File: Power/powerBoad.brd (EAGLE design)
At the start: 160 x 100 mm, 26 parts, among them CON1 MR30PW-M, CON2 XT30PW-M, CON3 XT30PW-M, U1 V7805-1000, U2 LD1117S33CTR, X1 JST-XH-06-PIN-LONG-PAD, X2 JST-XH-06-PIN-LONG-PAD, X3 JST-XH-06-PIN-LONG-PAD, X4 JST-XH-06-PIN-LONG-PAD

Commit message: some update 部品配置
# ==== Emojis ====
# ✨ :sparkles: Add new feature
# ✅  :white_check_mark: Update existing feature (not bug)
# ⚠️  :warning: Fix bug/error
# 🔥  :fire: Remove files or features
# ✏️ :pencil2: Fix typos
# 📝  :memo: Update documentation
# ♻️  :recycle: Dependencies update
# 🐧  :penguin: Improved the Linux
# 🍎  :apple: Improved the macOS
# 🔖 :bookmark: Add new library
# 🎉  :tada: Initial commit

# ==== Format ====
# :emoji: Subject
#
# Commit body...

# ==== Messages ====
# 新規(ファイル)機能追加: Add
# 機能修正、既存機能追加（バグではない): Update
# リファクタリング: Clean
# ファイル名変更:
# 削除など: Remove
# バグ修正: Fix
# バージョンアップ: Upgrade
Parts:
- removed J1: (no value), SparkFun-Connectors:JST-5-PTH
- removed MC1, MC33151: MC33151DR2G, MC33151DR2G:SOIC127P600X175-8N
- removed U$2: XT30UPB-M, XT30UPB-M:XT30UPB-M
- removed X1, X2, X3, X4: JST-XH-06-PIN-LONG-PAD, Rembrandt Electronics - JST XH Connectors v1-0:JST-XH-06-PACKAGE-LONG-PAD
- added CN1, CN2, CN3, CN4: (no value), jst-xh:S6B-XH-A
- added JP1, JP2: (no value), adafruit:1X06
- added U3, U4: MC33151DR2G, MC33151DR2G:SOIC127P600X175-8N
- moved C1 62.0 mm to (20.3, 26.7), turned to 90 degrees
- moved C3 52.4 mm to (20.3, 30.5), turned to 270 degrees
- moved C2 41.5 mm to (33.3, 38.1), turned to 180 degrees
- moved R1 41.2 mm to (60.6, 36.8)
- moved C4 41.2 mm to (60.6, 26.7)
- moved LED1 38.1 mm to (42.2, 25.4)
- moved D1 36.2 mm to (46.0, 21.6)
- moved R6 34.8 mm to (47.3, 38.1)
- moved R5 34.3 mm to (47.3, 35.6)
- moved CON1 34.1 mm to (40.6, 46.4), turned to 0 degrees
- moved KICK 10.1 mm to (26.7, 50.5), turned to 0 degrees
- moved U1 3.81 mm to (14.0, 29.2)
- moved CON2 2.93 mm to (41.3, 13.0)
- moved CON3 2.25 mm to (25.7, 13.0)
- moved C8 1.59 mm to (27.0, 22.9)
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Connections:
- removed net DR_PWM: CON1.1
- removed net TR_IN: KICK.4
- removed net VOLT_SIG: D1.C
- new net BAT: D1.C, JP1.1
- new net DRIB_PWM: CON1.1, JP1.4
- new net GPIO0: JP1.6
- new net PHOTO: JP1.5, KICK.4
- net +15V: now also JP2.1, U3.6, U4.6; no longer MC1.6, MC33151.6, U$2.P$2
- net +3V3: now also JP2.3
- net +5V: now also JP2.2
- net 5V: now also CN1.3, CN2.3, CN3.3, CN4.3; no longer X1.4, X2.4, X3.4, X4.4
- net CANH: now also CN1.2, CN2.2, CN3.2, CN4.2, JP1.2; no longer X1.5, X2.5, X3.5, X4.5
- net CANL: now also CN1.1, CN2.1, CN3.1, CN4.1, JP1.3; no longer X1.6, X2.6, X3.6, X4.6
- net GND: now also CN1.4, CN2.4, CN3.4, CN4.4, JP2.4, U3.3, U4.3; no longer MC1.3, MC33151.3, U$2.P$1, X1.3, X2.3, X3.3, X4.3
- net GVDD_IN: now also CN1.6, CN2.6, CN3.6, CN4.6; no longer X1.1, X2.1, X3.1, X4.1
- net KICK1: now also JP2.5, U3.2; no longer MC33151.2
- net KICK2: now also JP2.6, U4.2; no longer MC1.2
- net KICK_V: now also U3.7; no longer MC33151.7
- net KICK_V2: now also U4.7; no longer MC1.7
- net PVDD: now also CN1.5, CN2.5, CN3.5, CN4.5; no longer X1.2, X2.2, X3.2, X4.2
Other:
- board size 160 x 100 mm -> 67 x 59.7 mm

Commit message: POWERをいい感じにした
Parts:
- removed R5: 100k, rcl:0207/10
- removed R6: 470k, rcl:0207/10
- added LED3: (no value), led:CHIPLED_0603
- added R2: 470k, rcl:R0603
- added R3: 100k, rcl:R0603
- added R4: 5k, rcl:R0603
- LED1: device led:CHIP-LED0805 -> led:CHIPLED_0603
- R1: value (none) -> 1k
- moved R1 45.4 mm to (15.2, 38.4)
- moved C4 40.2 mm to (20.6, 30.2)
- moved D1 31.0 mm to (15.2, 17.8)
- moved LED1 30.7 mm to (15.2, 40.0), turned to 270 degrees
- moved C2 13.7 mm to (24.1, 27.9), turned to 90 degrees
- moved C1 13.1 mm to (7.94, 30.8), turned to 270 degrees
- moved C3 12.7 mm to (7.94, 27.6), turned to 90 degrees
- moved C5 8.72 mm to (29.8, 28.9), turned to 0 degrees
- moved U2 5.17 mm to (29.8, 36.8), turned to 90 degrees
- moved C6 3.70 mm to (22.5, 36.2)
- moved C8 3.13 mm to (25.7, 20.0)
- moved U3 0.95 mm to (31.1, 44.8)
- moved U4 0.95 mm to (23.2, 44.8)
- turned U1 to 90 degrees
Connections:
- net GVDD_IN renamed GVDD
- removed net +15V: C3.1, C8.+, CON1.2, CON2.+, CON3.+, JP2.1, R6.1, U1.1, U3.6, U4.6
- removed net 5V: CN1.3, CN2.3, CN3.3, CN4.3
- removed net LED: R1.2
- new net N$1: LED3.A, R4.1
- net +3V3: now also R1.2
- net +5V: now also CN1.3, CN2.3, CN3.3, CN4.3, R4.2
- net 2: now also R2.2, R3.2; no longer R5.2, R6.2
- net GND: now also LED3.C, R3.1; no longer R5.1
- net PVDD: now also C3.1, C8.+, CON1.2, CON2.+, CON3.+, JP2.1, R2.1, U1.1, U3.6, U4.6
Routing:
- net GND: track 0.00 -> 274.9 mm
- net PVDD: track 0.00 -> 246.1 mm
- net +5V: track 0.00 -> 42.5 mm
- net +3V3: track 0.00 -> 30.6 mm
- net 2: track 0.00 -> 4.90 mm
- net N$4: track 0.00 -> 1.63 mm
- net N$1: track 0.00 -> 1.63 mm

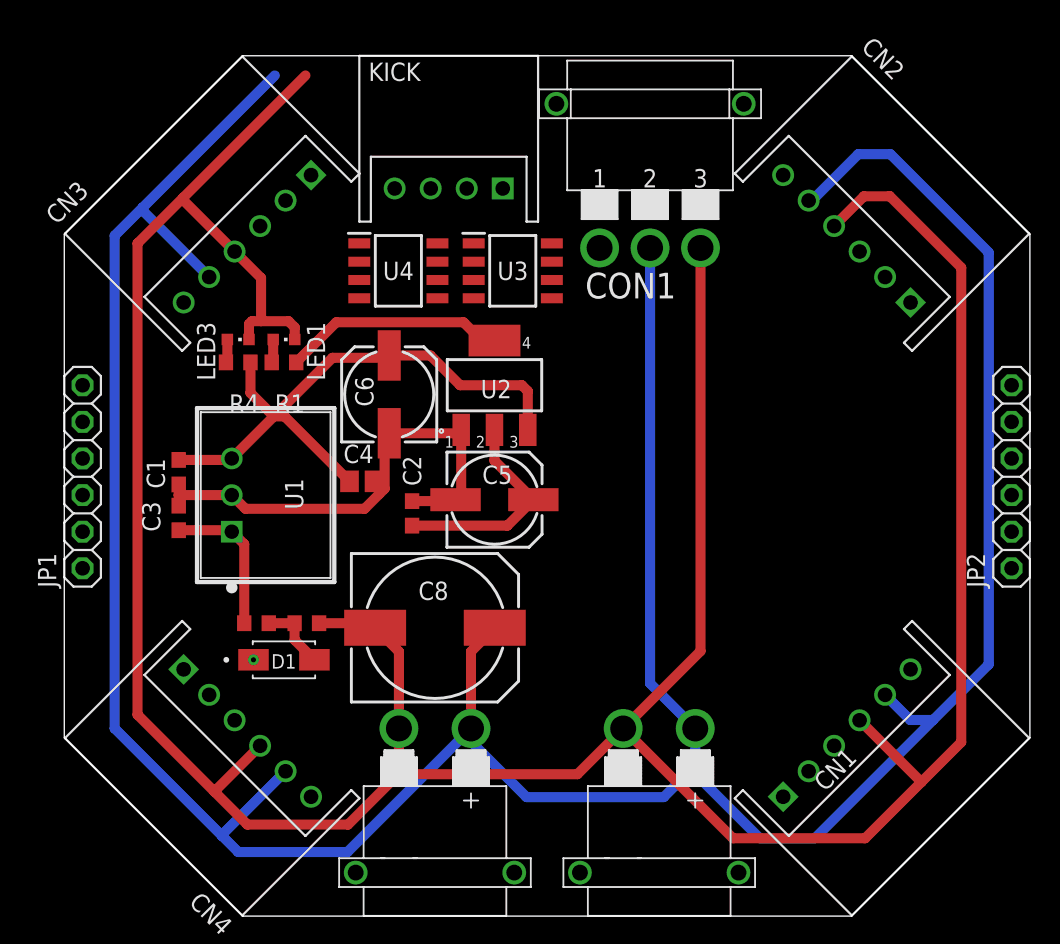
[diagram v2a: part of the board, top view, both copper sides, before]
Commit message: POWERの配線を進めた
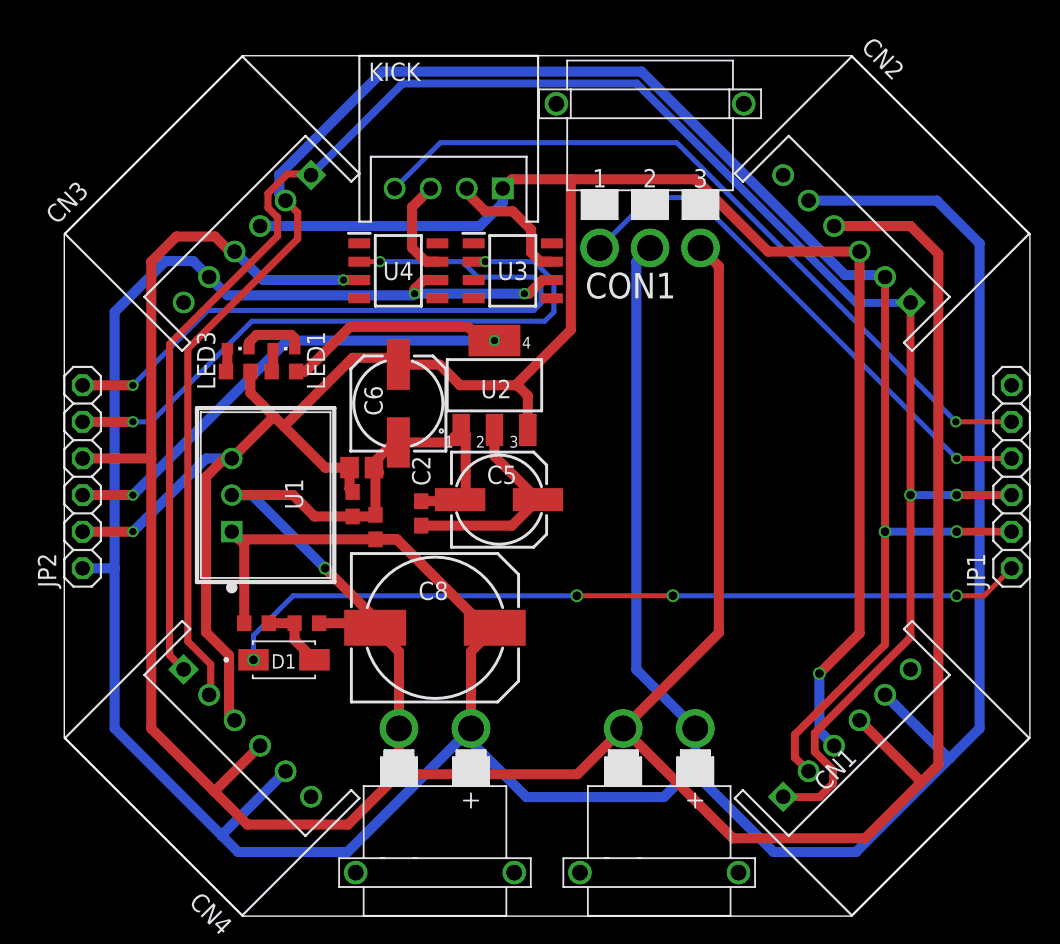
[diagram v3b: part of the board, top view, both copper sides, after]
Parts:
- moved JP1 64.5 mm to (65.7, 30.5)
- moved JP2 64.5 mm to (1.27, 30.5)
- moved C3 13.7 mm to (21.6, 27.0)
- moved C1 12.3 mm to (20.0, 28.6)
- moved C4 0.95 mm to (20.6, 31.1)
- moved C6 0.90 mm to (23.2, 35.6)
- moved LED1 0.64 mm to (15.2, 39.4)
- moved LED3 0.64 mm to (12.1, 39.4)
- moved C2 0.64 mm to (24.8, 27.9)
- moved R1 0.63 mm to (15.2, 37.8)
- moved R4 0.63 mm to (12.1, 37.8)
- moved C5 0.32 mm to (30.2, 28.9)
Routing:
- net CANL: track 0.00 -> 138.4 mm, vias 0 -> 2
- net CANH: track 0.00 -> 137.4 mm, vias 0 -> 2
- net +5V: track 42.5 -> 168.7 mm, vias 0 -> 2
- net BAT: track 0.00 -> 56.2 mm, vias 1 -> 4
- net PHOTO: track 0.00 -> 52.1 mm, vias 0 -> 1
- net KICK2: track 0.00 -> 48.1 mm, vias 0 -> 2
- net KICK1: track 0.00 -> 44.8 mm, vias 0 -> 2
- net PVDD: track 246.1 -> 286.7 mm, vias 0 -> 2
- net DRIB_PWM: track 0.00 -> 37.5 mm, vias 0 -> 1
- net +3V3: track 30.6 -> 63.4 mm, vias 0 -> 2
- net KICK_V: track 0.00 -> 9.12 mm
- net KICK_V2: track 0.00 -> 6.82 mm
- net GND: track 274.9 -> 273.4 mm, vias 0 -> 2

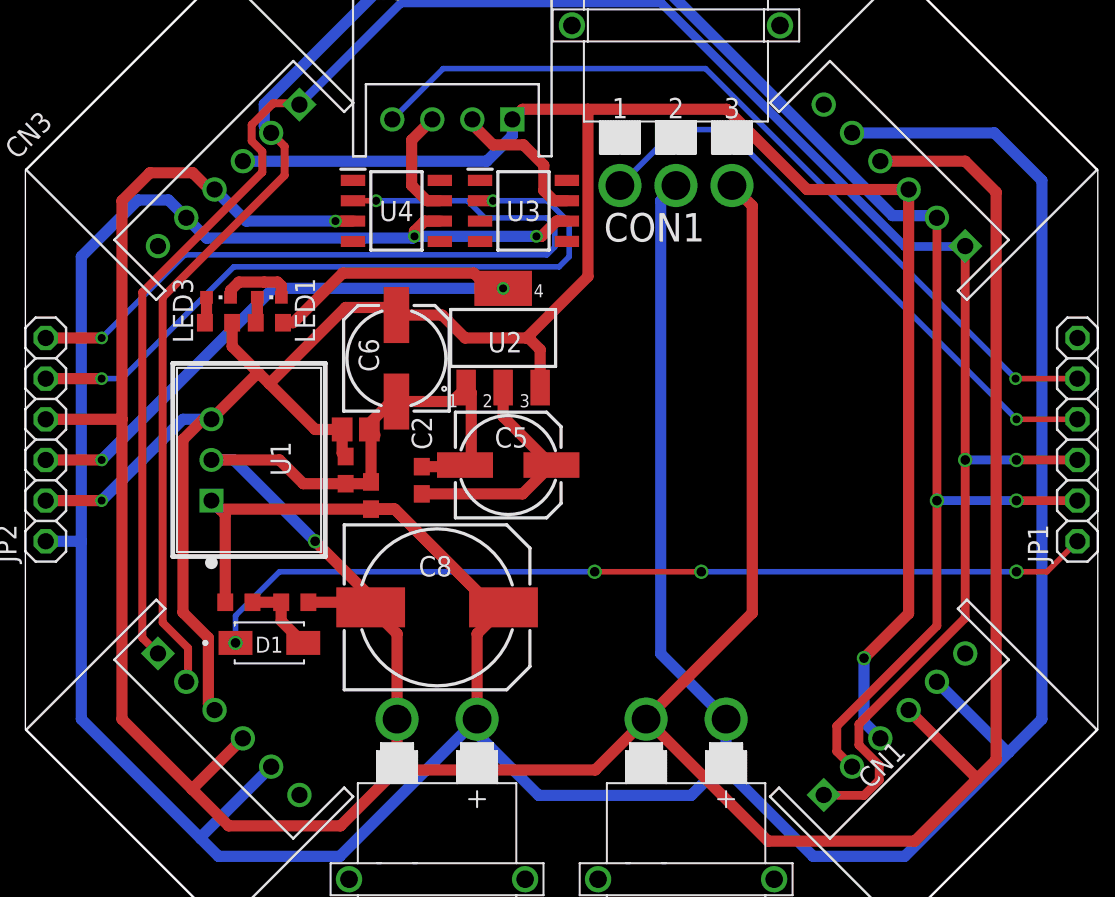
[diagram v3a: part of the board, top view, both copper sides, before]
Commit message: 可変レギュレータを追加して配線をやりきった
次はパワみ化させる
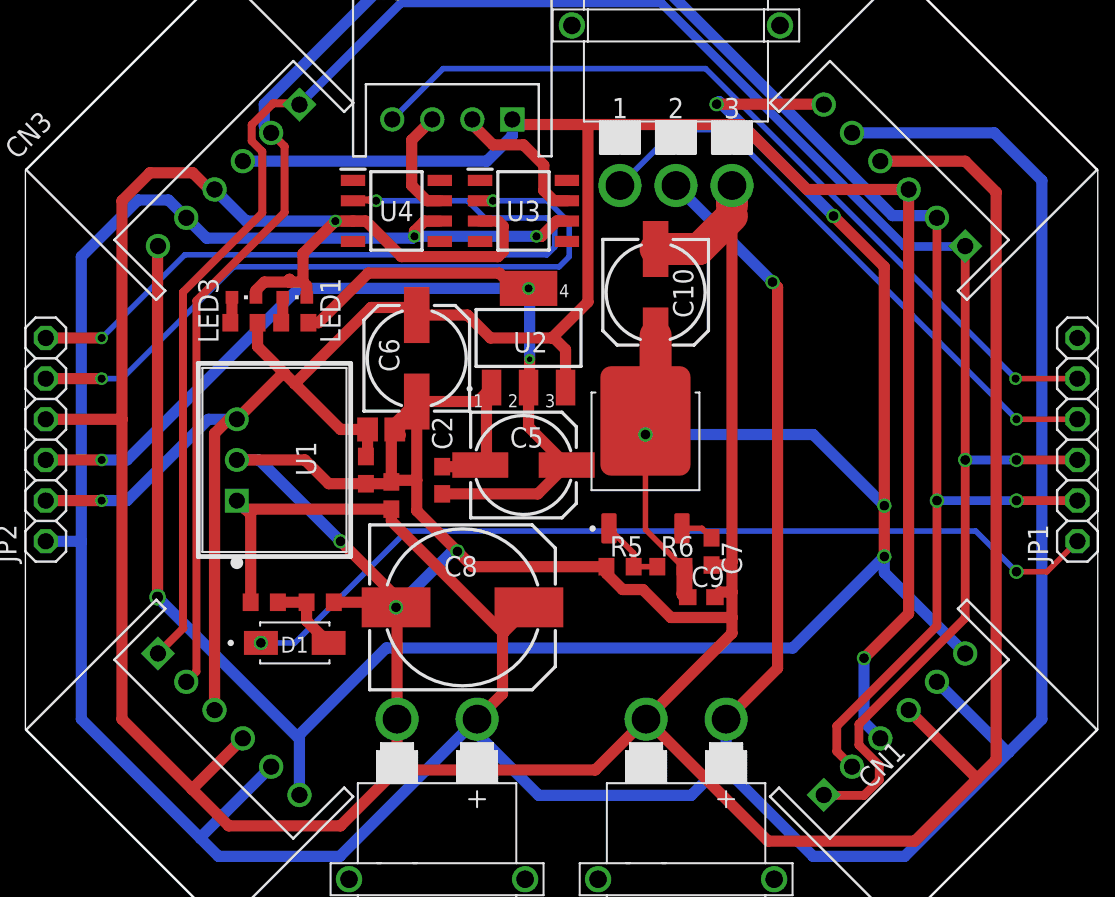
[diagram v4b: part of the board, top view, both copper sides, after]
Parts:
- added C10: 100u, rcl:153CLV-0605
- added C7, C9: 10u, rcl:C1608
- added R5: 3k, rcl:R0603
- added R6: 220, rcl:R0603
- added U$1: NJM317DL1, NJM317DL1:DPAK228P968X238-4N
- moved C4 1.59 mm to (22.2, 31.1)
- moved U2 1.59 mm to (31.4, 36.8)
- moved D1 1.59 mm to (16.8, 17.8)
- moved LED1 1.59 mm to (16.8, 39.4)
- moved LED3 1.59 mm to (13.7, 39.4)
- moved R1 1.59 mm to (16.8, 37.8)
- moved R4 1.59 mm to (13.7, 37.8)
- moved C8 1.59 mm to (27.3, 20.0)
- moved R2 1.59 mm to (14.9, 20.3)
- moved R3 1.59 mm to (18.4, 20.3)
- moved U1 1.59 mm to (15.6, 29.2)
- moved C6 1.27 mm to (24.4, 35.6)
- moved C1 1.27 mm to (21.3, 28.6)
- moved C2 1.27 mm to (26.0, 27.9)
- moved C3 1.27 mm to (22.9, 27.0)
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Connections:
- new net +15V: C7.1, U$1.3
- new net N$5: R5.2, R6.1, U$1.1
- net GND: now also C10.-, C7.2, C9.2, R5.1
- net GVDD: now also C10.+, C9.1, R6.2, U$1.2
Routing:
- net GVDD: track 0.00 -> 163.8 mm, vias 0 -> 6
- net GND: track 273.4 -> 334.3 mm, vias 2 -> 4
- net +3V3: track 63.4 -> 70.8 mm, vias 2 -> 3
- net PVDD: track 286.7 -> 279.5 mm, vias 2 -> 3
- net N$5: track 0.00 -> 4.51 mm
- net +15V: track 0.00 -> 2.09 mm
- net +5V: track 168.7 -> 167.1 mm
- net CANH: track 137.4 -> 136.1 mm
- net KICK2: track 48.1 -> 49.3 mm
- net CANL: track 138.4 -> 137.7 mm
- net BAT: track 56.2 -> 55.7 mm, vias 4 -> 2

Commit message: POWERみを増した
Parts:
- moved R2 4.24 mm to (19.1, 21.3)
- moved R3 4.24 mm to (22.5, 21.3)
- moved D1 4.24 mm to (21.0, 18.7)
- moved C10 4.18 mm to (43.5, 39.1)
- moved C2 4.18 mm to (30.2, 27.3)
- moved C3 4.18 mm to (27.0, 26.4)
- moved C8 4.18 mm to (31.4, 19.4)
- moved C5 4.18 mm to (35.2, 28.3)
- moved LED3 4.18 mm to (17.8, 38.7)
- moved R4 4.18 mm to (17.8, 37.1)
- moved U2 4.18 mm to (35.6, 36.2)
- moved U1 4.18 mm to (19.7, 28.6)
- moved C6 4.18 mm to (28.6, 34.9)
- moved U$1 4.18 mm to (42.9, 28.9)
- moved C1 4.18 mm to (25.4, 27.9)
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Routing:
- net GND: track 334.3 -> 370.4 mm, vias 4 -> 13
- net GVDD: track 163.8 -> 146.7 mm
- net +5V: track 167.1 -> 177.8 mm
- net CANL: track 137.7 -> 147.3 mm
- net CANH: track 136.1 -> 144.4 mm
- net KICK1: track 44.8 -> 52.2 mm
- net BAT: track 55.7 -> 50.7 mm
- net PVDD: track 279.5 -> 284.2 mm
- net +3V3: track 70.8 -> 74.6 mm
- net DRIB_PWM: track 37.5 -> 35.7 mm
- net KICK2: track 49.3 -> 50.8 mm
- net KICK_V: track 9.12 -> 8.19 mm
- net +15V: track 2.09 -> 1.41 mm
- net N$5: track 4.51 -> 3.89 mm
- added copper zone on layer 1, net GND
- added copper zone on layer 16, net GND
- added copper zone on layer 1, net PVDD
- added copper zone on layer 16, net PVDD

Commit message: POWERをした
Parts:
- moved C9 0.79 mm to (45.1, 20.0)
- moved R5 0.79 mm to (40.0, 21.9)
- moved R6 0.79 mm to (43.2, 21.9)
- moved C7 0.79 mm to (45.9, 22.1)
- moved C6 0.16 mm to (28.4, 34.9)
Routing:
- net GVDD: track 146.7 -> 148.6 mm
- net GND: track 370.4 -> 372.0 mm

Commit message: 配線の最適化をした
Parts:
- moved C2 1.75 mm to (31.9, 27.3)
- moved C1 1.43 mm to (26.8, 27.9)
- moved C5 1.27 mm to (36.5, 28.3)
- moved C7 1.27 mm to (47.1, 22.1)
- moved D1 1.27 mm to (22.2, 18.7)
- moved LED1 1.27 mm to (22.2, 38.7)
- moved R1 1.27 mm to (22.2, 37.1)
- moved R6 1.27 mm to (44.5, 21.9)
- moved U$1 1.27 mm to (44.1, 28.9)
- moved C3 1.27 mm to (28.3, 26.4)
- moved C4 1.27 mm to (27.6, 30.5)
- moved C6 1.27 mm to (29.7, 34.9)
- moved C8 1.27 mm to (32.7, 19.4)
- moved LED3 1.27 mm to (19.1, 38.7)
- moved R2 1.27 mm to (20.3, 21.3)
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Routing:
- net KICK1: track 52.2 -> 44.6 mm
- net +5V: track 177.8 -> 171.5 mm
- net GND: track 372.0 -> 366.3 mm, vias 13 -> 122
- net GVDD: track 148.6 -> 145.2 mm, vias 6 -> 7
- net CANL: track 147.3 -> 150.2 mm
- net PHOTO: track 52.1 -> 54.5 mm
- net N$2: track 0.00 -> 2.22 mm
- net N$3: track 0.00 -> 1.91 mm
- net CANH: track 144.4 -> 142.6 mm
- net PVDD: track 284.2 -> 282.6 mm
- net +3V3: track 74.6 -> 76.1 mm
- net BAT: track 50.7 -> 49.3 mm
- net KICK_V: track 8.19 -> 8.74 mm
- net DRIB_PWM: track 35.7 -> 36.3 mm
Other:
- board text added: "+3.3V"
- board text added: "+5V"
- board text added: "3V3"
- board text added: "5V"
- board text added: "BAT"
- board text added: "CANH"
- board text added: "CANL"
- board text added: "Drib"
- board text added: "GND"
- board text added: "KICK1"
- board text added: "KICK2"
- board text added: "PVDD"
- board text added: "Photo"
